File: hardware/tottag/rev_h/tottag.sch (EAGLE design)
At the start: 199 parts, among them J1 USB4110-GF-A, J2 DM3AT-SF-PEJM5, J3 TC2030-JLINK-NL-2SIDE, J4 TC2030-JLINK-NL-2SIDE, J5 MOLEX-PICO-SPOX-3SIDE, Q1 CSD75207W15, Q2 CSD75207W15, T1 HHM1595A1, U1 DW1000, U10 STM32F091CC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

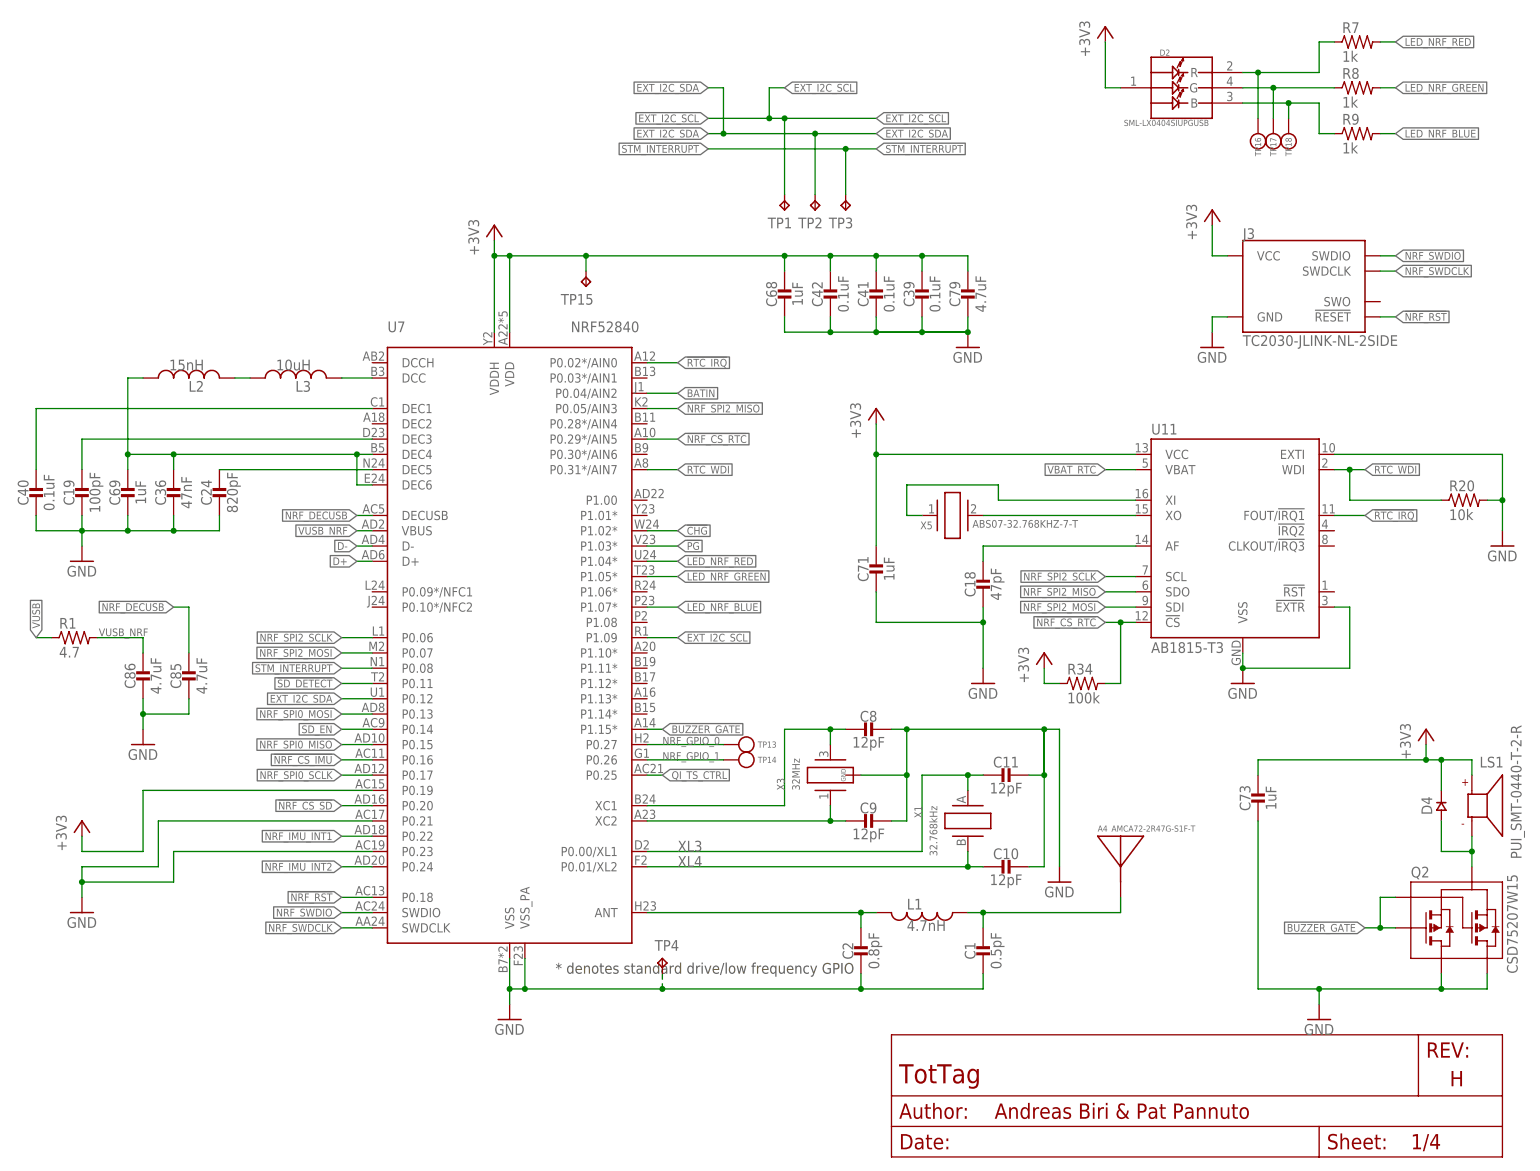
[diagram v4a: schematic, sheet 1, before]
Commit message: rev_h: move ID pins to low-freq GPIO pins
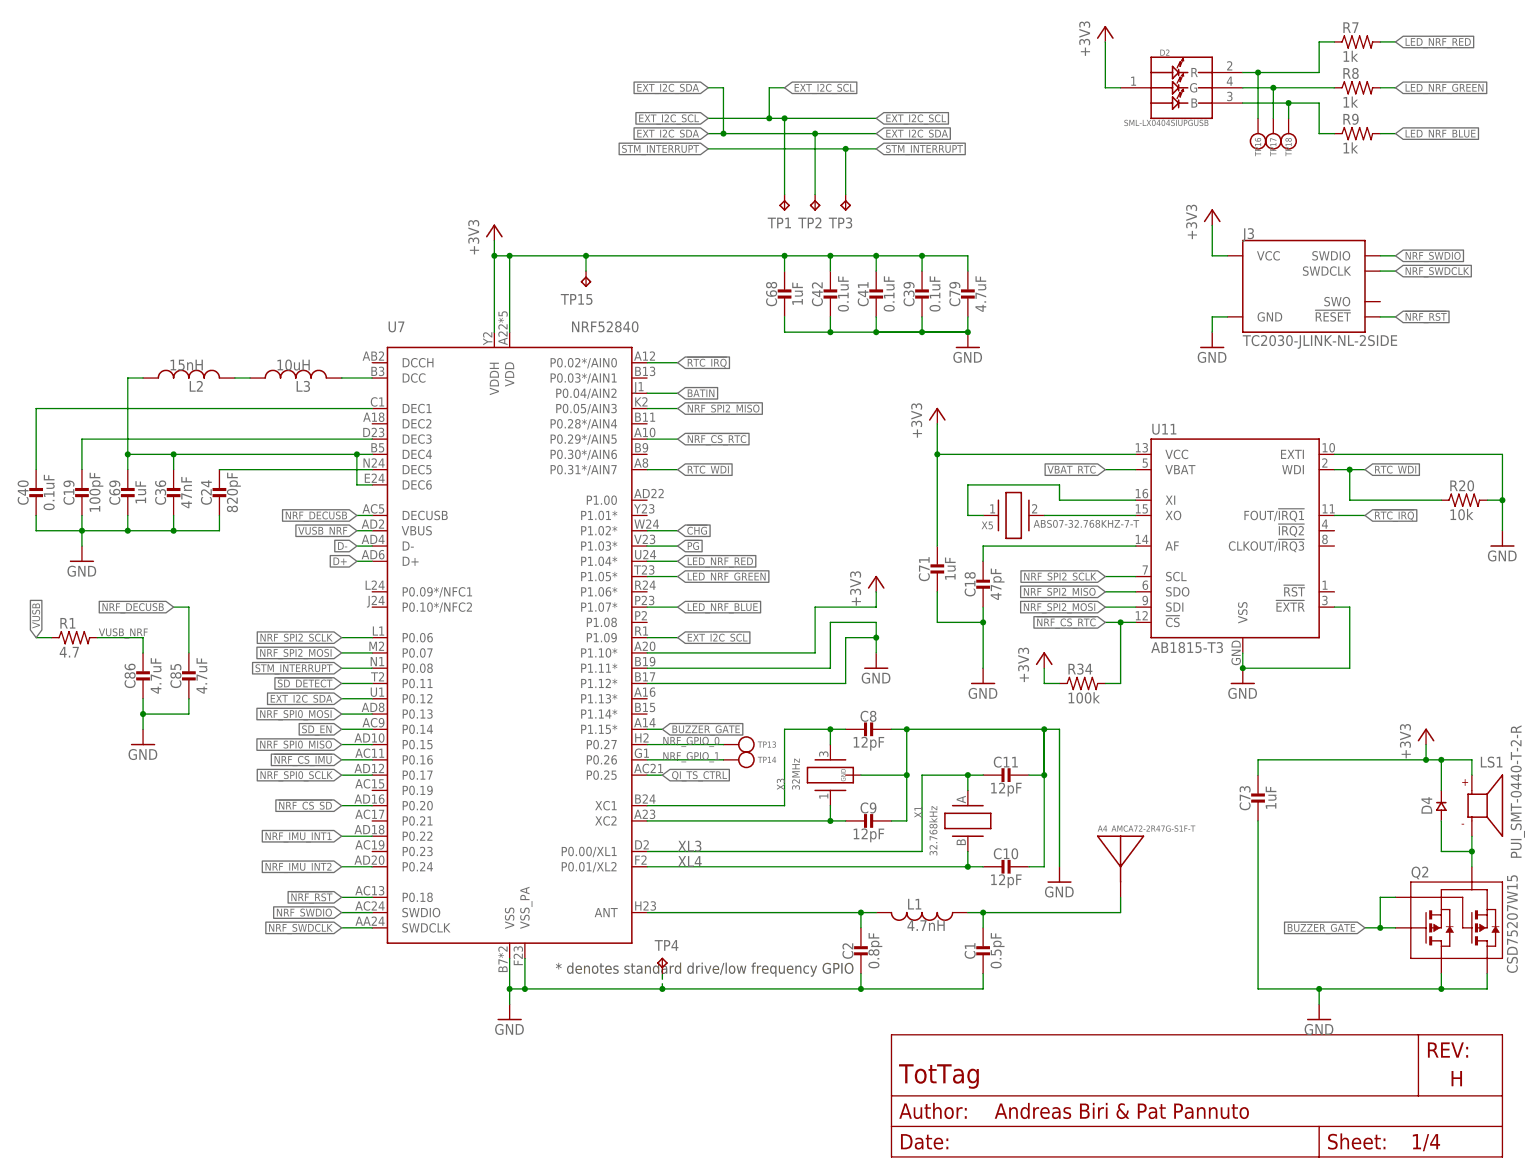
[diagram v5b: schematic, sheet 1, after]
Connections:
- net +3V3: now also U7.P1.10*; no longer U7.P0.19
- net GND: now also U7.P1.11*, U7.P1.12*; no longer U7.P0.21, U7.P0.23
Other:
- moved on the sheet: C71, X5
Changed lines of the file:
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@@
 <wire x1="177.8" y1="165.1" x2="177.8" y2="129.54" width="0.1524" layer="98" style="longdash"/>
 <wire x1="177.8" y1="129.54" x2="254" y2="129.54" width="0.1524" layer="98" style="longdash"/>
-<text x="149.86" y="121.92" size="3.81" layer="98">RTC</text>
-<wire x1="177.8" y1="129.54" x2="137.16" y2="129.54" width="0.1524" layer="98" style="longdash"/>
-<wire x1="137.16" y1="129.54" x2="137.16" y2="74.93" width="0.1524" layer="98" style="longdash"/>
-<wire x1="137.16" y1="74.93" x2="254" y2="74.93" width="0.1524" layer="98" style="longdash"/>
+<text x="160.02" y="124.46" size="3.81" layer="98">RTC</text>
+<wire x1="177.8" y1="129.54" x2="149.86" y2="129.54" width="0.1524" layer="98" style="longdash"/>
+<wire x1="149.86" y1="129.54" x2="149.86" y2="74.93" width="0.1524" layer="98" style="longdash"/>
+<wire x1="149.86" y1="74.93" x2="254" y2="74.93" width="0.1524" layer="98" style="longdash"/>
 <text x="180.34" y="160.02" size="3.81" layer="98">J-LINK</text>
 <text x="178.816" y="166.37" size="3.81" layer="98">LED</text>
@@
 <text x="143.256" y="27.178" size="1.016" layer="98" align="top-left">Matching network from datasheet.
 Note v1.1 datasheet updated values.</text>
-<text x="11.176" y="34.798" size="1.016" layer="98" align="top-center">Board Revision ID Pins
+<text x="140.716" y="100.838" size="1.016" layer="98" align="top-center">Board Revision ID Pins
 Rev H = 001
 </text>
-<wire x1="2.54" y1="30.48" x2="2.54" y2="58.42" width="0.1524" layer="98" style="longdash"/>
-<wire x1="19.304" y1="30.48" x2="19.304" y2="58.42" width="0.1524" layer="98" style="longdash"/>
-<wire x1="19.304" y1="30.48" x2="2.54" y2="30.48" width="0.1524" layer="98" style="longdash"/>
-<wire x1="19.304" y1="58.42" x2="2.54" y2="58.42" width="0.1524" layer="98" style="longdash"/>
+<wire x1="132.08" y1="76.2" x2="132.08" y2="101.6" width="0.1524" layer="98" style="longdash"/>
+<wire x1="148.844" y1="76.2" x2="148.844" y2="101.6" width="0.1524" layer="98" style="longdash"/>
+<wire x1="148.844" y1="76.2" x2="132.08" y2="76.2" width="0.1524" layer="98" style="longdash"/>
+<wire x1="148.844" y1="101.6" x2="132.08" y2="101.6" width="0.1524" layer="98" style="longdash"/>
 </plain>
 <instances>
@@
 <attribute name="VALUE" x="203.2" y="76.2" size="1.778" layer="96"/>
 </instance>
-<instance part="X5" gate="G$1" x="157.48" y="106.68" smashed="yes">
-<attribute name="NAME" x="154.178" y="105.664" size="1.27" layer="95" rot="R180"/>
-<attribute name="VALUE" x="160.782" y="104.648" size="1.27" layer="96"/>
-</instance>
-<instance part="C71" gate="G$1" x="144.78" y="99.06" smashed="yes">
-<attribute name="DIGIKEY" x="144.78" y="99.06" size="1.778" layer="96" display="off"/>
-<attribute name="MPN" x="144.78" y="99.06" size="1.778" layer="96" display="off"/>
-<attribute name="NAME" x="143.51" y="97.79" size="1.778" layer="95" ratio="12" rot="R90" align="bottom-center"/>
-<attribute name="VALUE" x="146.05" y="97.79" size="1.778" layer="96" ratio="12" rot="R270" align="bottom-center"/>
+<instance part="X5" gate="G$1" x="167.64" y="106.68" smashed="yes">
+<attribute name="NAME" x="164.338" y="105.664" size="1.27" layer="95" rot="R180"/>
+<attribute name="VALUE" x="170.942" y="104.648" size="1.27" layer="96"/>
+</instance>
+<instance part="C71" gate="G$1" x="154.94" y="99.06" smashed="yes">
+<attribute name="DIGIKEY" x="154.94" y="99.06" size="1.778" layer="96" display="off"/>
+<attribute name="MPN" x="154.94" y="99.06" size="1.778" layer="96" display="off"/>
+<attribute name="NAME" x="153.67" y="97.79" size="1.778" layer="95" ratio="12" rot="R90" align="bottom-center"/>
+<attribute name="VALUE" x="156.21" y="97.79" size="1.778" layer="96" ratio="12" rot="R270" align="bottom-center"/>
 </instance>
 <instance part="R20" gate="G$1" x="243.84" y="109.22" smashed="yes">
@@
 <attribute name="VALUE" x="246.38" y="99.06" size="1.778" layer="96"/>
 </instance>
-<instance part="P+3" gate="P1" x="144.78" y="124.46" smashed="yes">
-<attribute name="VALUE" x="142.24" y="119.38" size="1.778" layer="96" rot="R90"/>
+<instance part="P+3" gate="P1" x="154.94" y="124.46" smashed="yes">
+<attribute name="VALUE" x="152.4" y="119.38" size="1.778" layer="96" rot="R90"/>
 </instance>
 <instance part="J3" gate="G$1" x="215.9" y="144.78" smashed="yes">
@@
 <attribute name="NAME" x="213.36" y="169.545" size="1.016" layer="95" ratio="12" rot="R90" align="center-right"/>
 </instance>
-<instance part="P+6" gate="P1" x="12.7" y="55.88" smashed="yes">
-<attribute name="VALUE" x="10.16" y="50.8" size="1.778" layer="96" rot="R90"/>
-</instance>
-<instance part="GND9" gate="1" x="12.7" y="40.64" smashed="yes">
-<attribute name="VALUE" x="10.16" y="38.1" size="1.778" layer="96"/>
+<instance part="P+6" gate="P1" x="144.78" y="96.52" smashed="yes">
+<attribute name="VALUE" x="142.24" y="91.44" size="1.778" layer="96" rot="R90"/>
+</instance>
+<instance part="GND9" gate="1" x="144.78" y="81.28" smashed="yes">
+<attribute name="VALUE" x="142.24" y="78.74" size="1.778" layer="96"/>
 </instance>
 <instance part="P+7" gate="P1" x="172.72" y="83.82" smashed="yes">
@@
 <pinref part="GND13" gate="1" pin="GND"/>
 <wire x1="162.56" y1="88.9" x2="162.56" y2="81.28" width="0.1524" layer="91"/>
-<wire x1="144.78" y1="93.98" x2="144.78" y2="88.9" width="0.1524" layer="91"/>
+<wire x1="154.94" y1="93.98" x2="154.94" y2="88.9" width="0.1524" layer="91"/>
 <junction x="162.56" y="88.9"/>
-<wire x1="144.78" y1="88.9" x2="162.56" y2="88.9" width="0.1524" layer="91"/>
+<wire x1="154.94" y1="88.9" x2="162.56" y2="88.9" width="0.1524" layer="91"/>
 <pinref part="C71" gate="G$1" pin="2"/>
 </segment>
@@
 </segment>
 <segment>
-<pinref part="U7" gate="G$1" pin="P0.23"/>
-<wire x1="60.96" y1="50.8" x2="27.94" y2="50.8" width="0.1524" layer="91"/>
-<wire x1="27.94" y1="50.8" x2="27.94" y2="45.72" width="0.1524" layer="91"/>
-<wire x1="27.94" y1="45.72" x2="12.7" y2="45.72" width="0.1524" layer="91"/>
 <pinref part="GND9" gate="1" pin="GND"/>
-<wire x1="12.7" y1="45.72" x2="12.7" y2="43.18" width="0.1524" layer="91"/>
-<pinref part="U7" gate="G$1" pin="P0.21"/>
-<wire x1="60.96" y1="55.88" x2="25.4" y2="55.88" width="0.1524" layer="91"/>
-<wire x1="25.4" y1="55.88" x2="25.4" y2="48.26" width="0.1524" layer="91"/>
-<wire x1="25.4" y1="48.26" x2="12.7" y2="48.26" width="0.1524" layer="91"/>
-<wire x1="12.7" y1="48.26" x2="12.7" y2="45.72" width="0.1524" layer="91"/>
-<junction x="12.7" y="45.72"/>
+<pinref part="U7" gate="G$1" pin="P1.11*"/>
+<wire x1="144.78" y1="88.9" x2="144.78" y2="86.36" width="0.1524" layer="91"/>
+<wire x1="144.78" y1="86.36" x2="144.78" y2="83.82" width="0.1524" layer="91"/>
+<wire x1="106.68" y1="81.28" x2="137.16" y2="81.28" width="0.1524" layer="91"/>
+<wire x1="137.16" y1="81.28" x2="137.16" y2="88.9" width="0.1524" layer="91"/>
+<wire x1="137.16" y1="88.9" x2="144.78" y2="88.9" width="0.1524" layer="91"/>
+<pinref part="U7" gate="G$1" pin="P1.12*"/>
+<wire x1="106.68" y1="78.74" x2="139.7" y2="78.74" width="0.1524" layer="91"/>
+<wire x1="139.7" y1="78.74" x2="139.7" y2="86.36" width="0.1524" layer="91"/>
+<wire x1="139.7" y1="86.36" x2="144.78" y2="86.36" width="0.1524" layer="91"/>
+<junction x="144.78" y="86.36"/>
 </segment>
 </net>
@@
 <segment>
 <pinref part="U11" gate="G$1" pin="VCC"/>
-<wire x1="187.96" y1="116.84" x2="144.78" y2="116.84" width="0.1524" layer="91"/>
+<wire x1="187.96" y1="116.84" x2="154.94" y2="116.84" width="0.1524" layer="91"/>
 <pinref part="C71" gate="G$1" pin="1"/>
-<wire x1="144.78" y1="116.84" x2="144.78" y2="101.6" width="0.1524" layer="91"/>
-<wire x1="144.78" y1="121.92" x2="144.78" y2="116.84" width="0.1524" layer="91"/>
-<junction x="144.78" y="116.84"/>
+<wire x1="154.94" y1="116.84" x2="154.94" y2="101.6" width="0.1524" layer="91"/>
+<wire x1="154.94" y1="121.92" x2="154.94" y2="116.84" width="0.1524" layer="91"/>
+<junction x="154.94" y="116.84"/>
 <pinref part="P+3" gate="P1" pin="+3V3"/>
 </segment>
@@
 </segment>
 <segment>
-<pinref part="U7" gate="G$1" pin="P0.19"/>
-<wire x1="60.96" y1="60.96" x2="22.86" y2="60.96" width="0.1524" layer="91"/>
-<wire x1="22.86" y1="60.96" x2="22.86" y2="50.8" width="0.1524" layer="91"/>
-<wire x1="22.86" y1="50.8" x2="12.7" y2="50.8" width="0.1524" layer="91"/>
 <pinref part="P+6" gate="P1" pin="+3V3"/>
-<wire x1="12.7" y1="50.8" x2="12.7" y2="53.34" width="0.1524" layer="91"/>
+<wire x1="144.78" y1="91.44" x2="144.78" y2="93.98" width="0.1524" layer="91"/>
+<pinref part="U7" gate="G$1" pin="P1.10*"/>
+<wire x1="106.68" y1="83.82" x2="134.62" y2="83.82" width="0.1524" layer="91"/>
+<wire x1="134.62" y1="83.82" x2="134.62" y2="91.44" width="0.1524" layer="91"/>
+<wire x1="134.62" y1="91.44" x2="144.78" y2="91.44" width="0.1524" layer="91"/>
 </segment>
 <segment>
@@
 <net name="N$41" class="0">
 <segment>
-<wire x1="149.86" y1="111.76" x2="165.1" y2="111.76" width="0.1524" layer="91"/>
-<wire x1="165.1" y1="111.76" x2="165.1" y2="109.22" width="0.1524" layer="91"/>
+<wire x1="160.02" y1="111.76" x2="175.26" y2="111.76" width="0.1524" layer="91"/>
+<wire x1="175.26" y1="111.76" x2="175.26" y2="109.22" width="0.1524" layer="91"/>
 <pinref part="U11" gate="G$1" pin="XI"/>
-<wire x1="165.1" y1="109.22" x2="187.96" y2="109.22" width="0.1524" layer="91"/>
+<wire x1="175.26" y1="109.22" x2="187.96" y2="109.22" width="0.1524" layer="91"/>
 <pinref part="X5" gate="G$1" pin="1"/>
-<wire x1="149.86" y1="111.76" x2="149.86" y2="106.68" width="0.1524" layer="91"/>
-<wire x1="149.86" y1="106.68" x2="152.4" y2="106.68" width="0.1524" layer="91"/>
+<wire x1="160.02" y1="111.76" x2="160.02" y2="106.68" width="0.1524" layer="91"/>
+<wire x1="160.02" y1="106.68" x2="162.56" y2="106.68" width="0.1524" layer="91"/>
 </segment>
 </net>
@@
 <pinref part="X5" gate="G$1" pin="2"/>
 <pinref part="U11" gate="G$1" pin="XO"/>
-<wire x1="187.96" y1="106.68" x2="162.56" y2="106.68" width="0.1524" layer="91"/>
-</segment>
-</net>
+<wire x1="187.96" y1="106.68" x2="172.72" y2="106.68" width="0.1524" layer="91"/>
+</segment>
+</net>

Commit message: rev_h: add test points for all buses
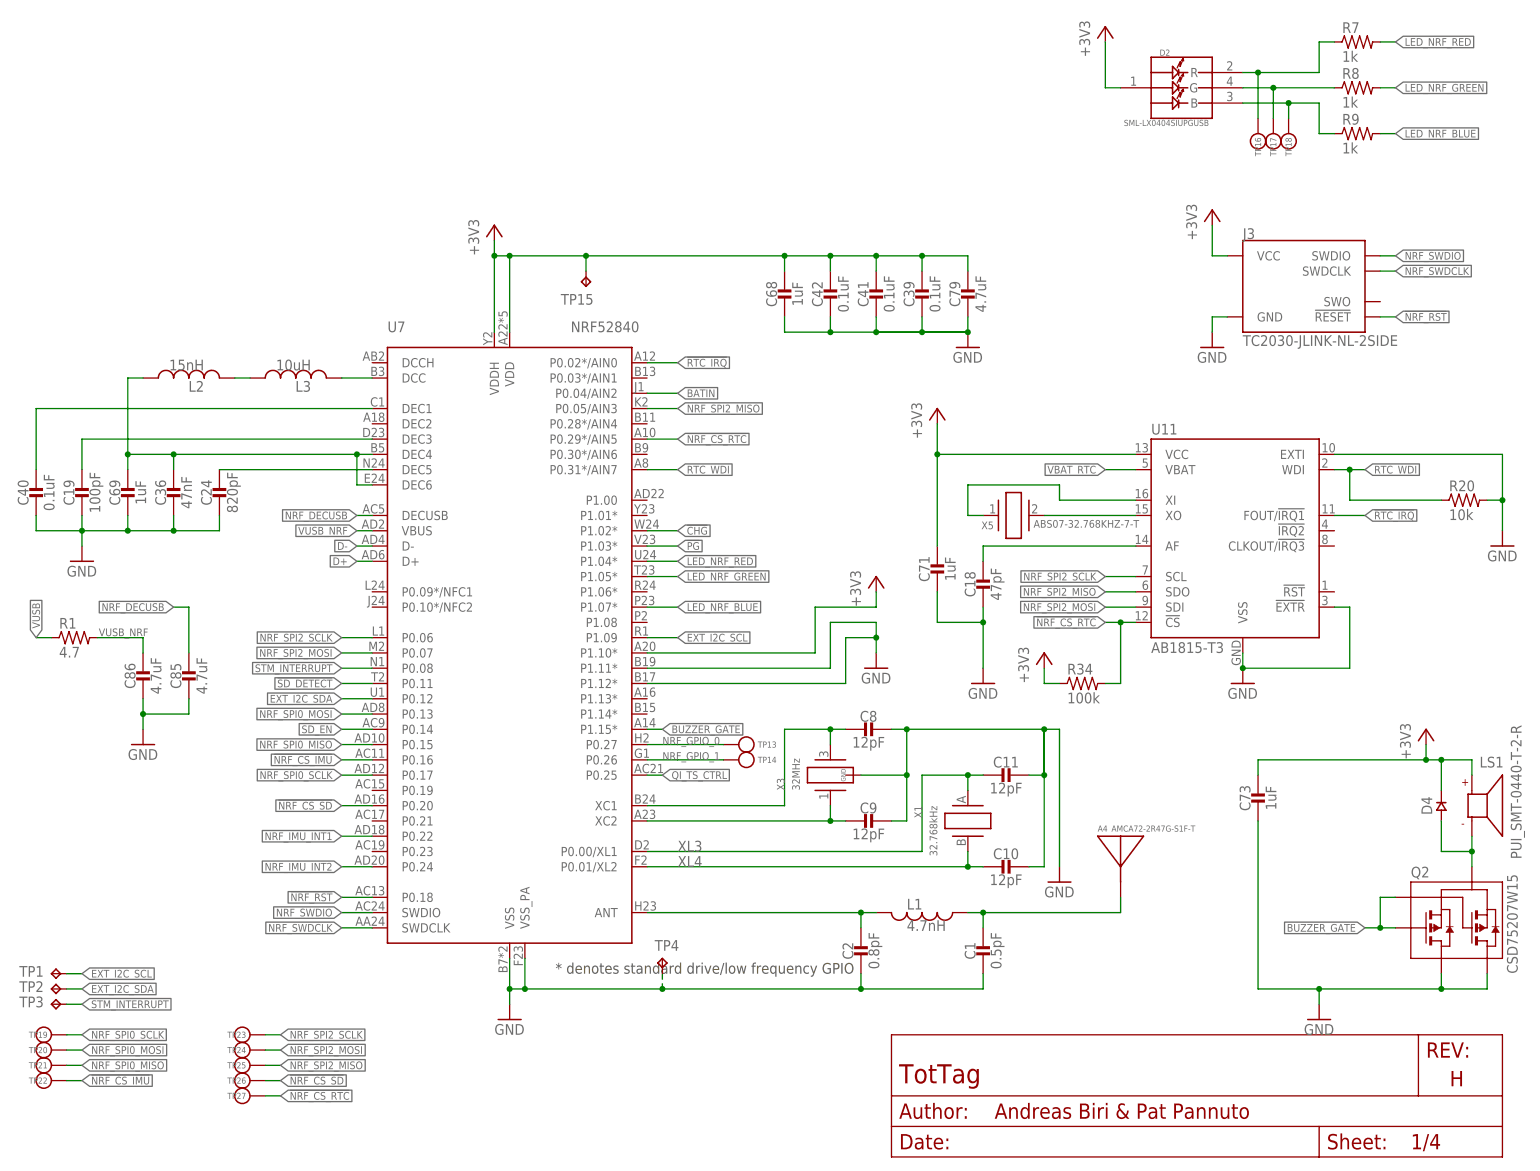
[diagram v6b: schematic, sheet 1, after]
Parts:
- added TP19, TP20, TP21, TP22, TP23, TP24, TP25, TP26, TP27: TEST-POINT, headers:TEST-POINT
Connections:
- net !NRF_CS_IMU: now also TP22.TESTPOINT
- net !NRF_CS_RTC: now also TP27.TESTPOINT
- net !NRF_CS_SD: now also TP26.TESTPOINT
- net NRF_SPI0_MISO: now also TP21.TESTPOINT
- net NRF_SPI0_MOSI: now also TP20.TESTPOINT
- net NRF_SPI0_SCLK: now also TP19.TESTPOINT
- net NRF_SPI2_MISO: now also TP25.TESTPOINT
- net NRF_SPI2_MOSI: now also TP24.TESTPOINT
- net NRF_SPI2_SCLK: now also TP23.TESTPOINT
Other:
- moved on the sheet: TP1, TP2, TP3
